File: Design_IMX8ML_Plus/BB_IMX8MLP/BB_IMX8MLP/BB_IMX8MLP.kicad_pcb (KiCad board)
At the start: 2 copper layers, 125 x 100 mm, 207 parts, among them J1 DF40C-100DP-0.4V_51_, J10 Barrel_Jack, J11 SIM_Card, J2 DF40C-100DP-0.4V_51_, J3 DF40C-100DP-0.4V_51_, J4 DF40C-100DP-0.4V_51_, J5 RJ45_JK0654219, J6 RJ45_JK0654219, J7 HDMI_A, J8 Bus_PCI_Express_Mini, J9 GSB311231HR, Q1 PMDT290UCE, Q2 NTMFS5C670NLT1G, Q3 NTMFS5C670NLT1G, Q4 PMDT290UCE, SW1 Power ON/OFF, SW2 RESET, SW3 RECOVERY, U1 KSZ9131RNXI, U10 PCMF3USB3S, U17 FXMA2102L8X, U2 HDMI2C1-14HDS, U20 INA219BxD, U21 PCMF3USB3S, U22 PCMF3USB3S, U23 PCMF3USB3S, U3 USB5744_2G, U30 NAU88C22YG, U4 LTC4368IDD-1_PBF, U5 AOZ2261AQI-15, U6 NCV4274CST50T3G, U7 AOZ2261AQI-15, U8 LTC2954CDDB-1-TRMPBF, U9 PCMF3USB3S, Y1 25MHz, Y2 25MHz

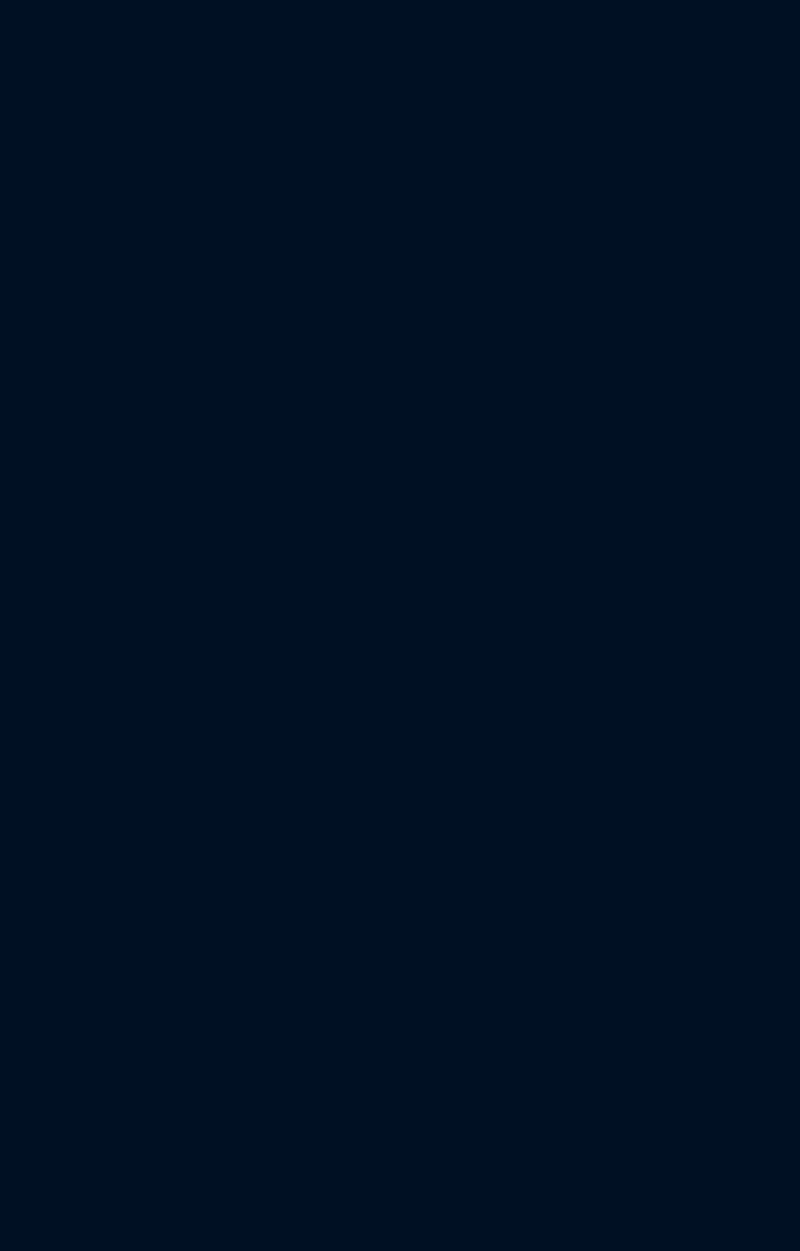
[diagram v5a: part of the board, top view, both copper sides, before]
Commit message: Adds audio interface
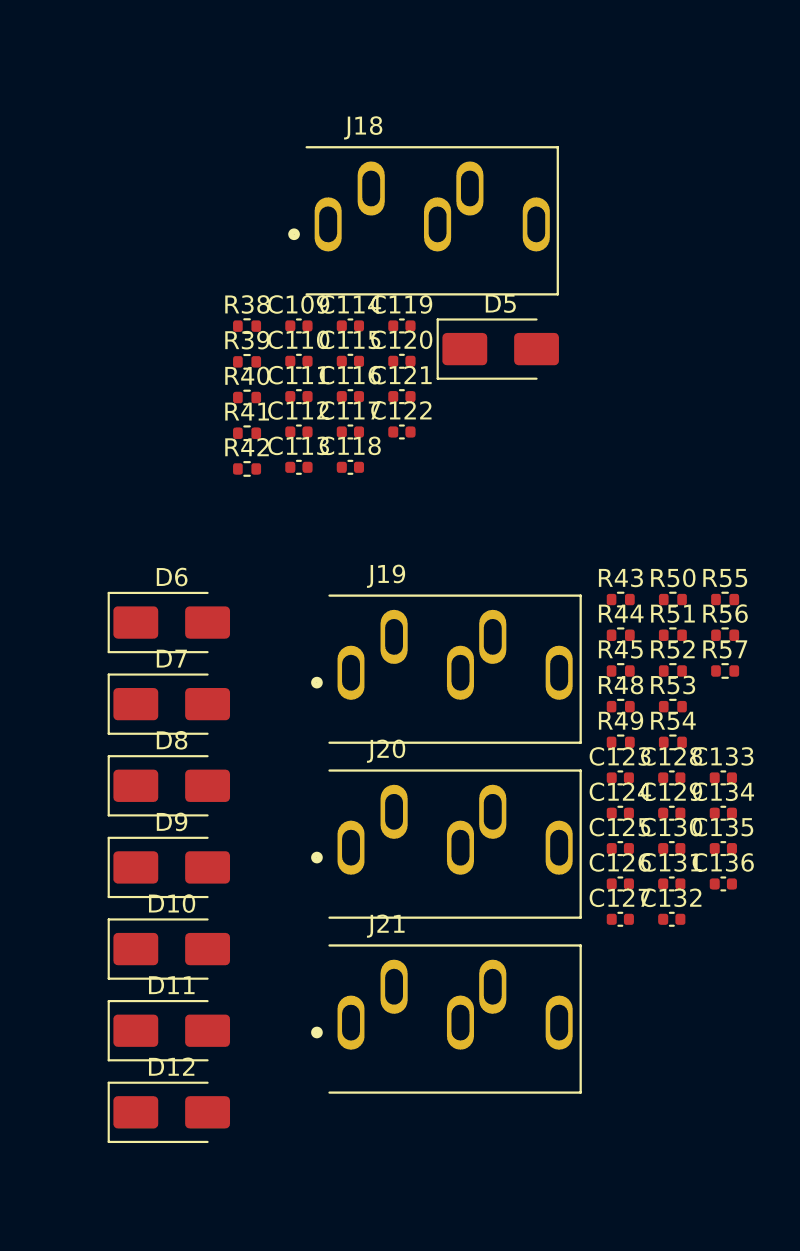
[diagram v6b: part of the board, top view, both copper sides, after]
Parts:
- added C109: 220pF, Capacitor_SMD:C_0402_1005Metric, F.Cu at (250.7, 74.9)
- added C110: 100nF, Capacitor_SMD:C_0402_1005Metric, F.Cu at (250.7, 76.8)
- added C111: 100nF, Capacitor_SMD:C_0402_1005Metric, F.Cu at (250.7, 78.8)
- added C112: 4.7uF, Capacitor_SMD:C_0402_1005Metric, F.Cu at (250.7, 80.8)
- added C113: 100nF, Capacitor_SMD:C_0402_1005Metric, F.Cu at (250.7, 82.7)
- added C114: 4.7uF, Capacitor_SMD:C_0402_1005Metric, F.Cu at (253.5, 74.9)
- added C115: 4.7uF, Capacitor_SMD:C_0402_1005Metric, F.Cu at (253.5, 76.8)
- added C116: 4.7uF, Capacitor_SMD:C_0402_1005Metric, F.Cu at (253.5, 78.8)
- added C117: 100nF, Capacitor_SMD:C_0402_1005Metric, F.Cu at (253.5, 80.8)
- added C118: 100nF, Capacitor_SMD:C_0402_1005Metric, F.Cu at (253.5, 82.7)
- added C119: 4.7uF, Capacitor_SMD:C_0402_1005Metric, F.Cu at (256.4, 74.9)
- added C120: 100nF, Capacitor_SMD:C_0402_1005Metric, F.Cu at (256.4, 76.8)
- added C121: 100nF, Capacitor_SMD:C_0402_1005Metric, F.Cu at (256.4, 78.8)
- added C122: 4.7uF, Capacitor_SMD:C_0402_1005Metric, F.Cu at (256.4, 80.8)
- added C123: 220pF, Capacitor_SMD:C_0402_1005Metric, F.Cu at (268.6, 100.0)
- added C124: 220pF, Capacitor_SMD:C_0402_1005Metric, F.Cu at (268.6, 102.0)
- added C125: 220pF, Capacitor_SMD:C_0402_1005Metric, F.Cu at (268.6, 104.0)
- added C126: 220pF, Capacitor_SMD:C_0402_1005Metric, F.Cu at (268.6, 106.0)
- added C127: 220pF, Capacitor_SMD:C_0402_1005Metric, F.Cu at (268.6, 107.9)
- added C128: 220pF, Capacitor_SMD:C_0402_1005Metric, F.Cu at (271.5, 100.0)
- added C129: 220pF, Capacitor_SMD:C_0402_1005Metric, F.Cu at (271.5, 102.0)
- added C130: 220pF, Capacitor_SMD:C_0402_1005Metric, F.Cu at (271.5, 104.0)
- added C131: 1uF, Capacitor_SMD:C_0402_1005Metric, F.Cu at (271.5, 106.0)
- added C132: 1uf, Capacitor_SMD:C_0402_1005Metric, F.Cu at (271.5, 107.9)
- added C133: 1uf, Capacitor_SMD:C_0402_1005Metric, F.Cu at (274.3, 100.0)
- added C134: 1uF, Capacitor_SMD:C_0402_1005Metric, F.Cu at (274.3, 102.0)
- added C135: 1uf, Capacitor_SMD:C_0402_1005Metric, F.Cu at (274.3, 104.0)
- added C136: 1uF, Capacitor_SMD:C_0402_1005Metric, F.Cu at (274.3, 106.0)
- added D10: SS3200, Diode_SMD:D_SMA, F.Cu at (243.6, 109.6)
- added D11: SS3200, Diode_SMD:D_SMA, F.Cu at (243.6, 114.1)
- added D12: SS3200, Diode_SMD:D_SMA, F.Cu at (243.6, 118.7)
- added D5: SS3200, Diode_SMD:D_SMA, F.Cu at (261.9, 76.2)
- added D6: SS3200, Diode_SMD:D_SMA, F.Cu at (243.6, 91.4)
- added D7: SS3200, Diode_SMD:D_SMA, F.Cu at (243.6, 95.9)
- added D8: SS3200, Diode_SMD:D_SMA, F.Cu at (243.6, 100.5)
- added D9: SS3200, Diode_SMD:D_SMA, F.Cu at (243.6, 105.0)
- added J18: MIC IN-Pink, _W_SBC:SJ1-3535NG-PI, F.Cu at (252.3, 69.2)
- added J19: Head Out -Green, _W_SBC:SJ1-3535NG-PI, F.Cu at (253.6, 94.2)
- added J20: Line -in -Blue, _W_SBC:SJ1-3535NG-PI, F.Cu at (253.6, 103.9)
- added J21: AUX OUT -Black, _W_SBC:SJ1-3535NG-PI, F.Cu at (253.6, 113.7)
- added R38: 47K, Resistor_SMD:R_0402_1005Metric, F.Cu at (247.8, 74.9)
- added R39: 120R@100MHz, Resistor_SMD:R_0402_1005Metric, F.Cu at (247.8, 76.9)
- added R40: 120R@100MHz, Resistor_SMD:R_0402_1005Metric, F.Cu at (247.8, 78.8)
- added R41: 120R@100MHz, Resistor_SMD:R_0402_1005Metric, F.Cu at (247.8, 80.8)
- added R42: 120R@100MHz, Resistor_SMD:R_0402_1005Metric, F.Cu at (247.8, 82.8)
- added R43: 47k, Resistor_SMD:R_0402_1005Metric, F.Cu at (268.6, 90.1)
- added R44: 2.2k, Resistor_SMD:R_0402_1005Metric, F.Cu at (268.6, 92.1)
- added R45: 2.2K, Resistor_SMD:R_0402_1005Metric, F.Cu at (268.6, 94.1)
- added R48: 47k, Resistor_SMD:R_0402_1005Metric, F.Cu at (268.6, 96.1)
- added R49: 47K, Resistor_SMD:R_0402_1005Metric, F.Cu at (268.6, 98.1)
- added R50: 100, Resistor_SMD:R_0402_1005Metric, F.Cu at (271.5, 90.1)
- added R51: 100, Resistor_SMD:R_0402_1005Metric, F.Cu at (271.5, 92.1)
- added R52: 4.7k, Resistor_SMD:R_0402_1005Metric, F.Cu at (271.5, 94.1)
- added R53: 4.7K, Resistor_SMD:R_0402_1005Metric, F.Cu at (271.5, 96.1)
- added R54: 10k, Resistor_SMD:R_0402_1005Metric, F.Cu at (271.5, 98.1)
- added R55: 10K, Resistor_SMD:R_0402_1005Metric, F.Cu at (274.4, 90.1)
- added R56: 100, Resistor_SMD:R_0402_1005Metric, F.Cu at (274.4, 92.1)
- added R57: 100, Resistor_SMD:R_0402_1005Metric, F.Cu at (274.4, 94.1)
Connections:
- U30 pad 12: unconnected-(U30-VSSD-Pad12) -> LVDS0_D2_N
- U30 pad 13: unconnected-(U30-VDDC-Pad13) -> /Audio/1v8_AAP
- U30 pad 14: unconnected-(U30-VDDB-Pad14) -> /Audio/1v8_AAP
- U30 pad 24: unconnected-(U30-VSSSPK-Pad24) -> LVDS0_D2_N
- U30 pad 26: unconnected-(U30-VDDSPK-Pad26) -> /Audio/3v3_AAP
- U30 pad 28: unconnected-(U30-VSSA-Pad28) -> LVDS0_D2_N
- U30 pad 31: unconnected-(U30-VDDA-Pad31) -> /Audio/3v3_AAP
- U30 pad 33: unconnected-(U30-EXP-Pad33) -> LVDS0_D2_N

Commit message: Review
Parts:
- added C137: 1uf, Capacitor_SMD:C_0402_1005Metric, F.Cu at (24.9, 10.4)
- added C138: 1uF, Capacitor_SMD:C_0402_1005Metric, F.Cu at (24.9, 12.4)
- added C139: 100nF, Capacitor_SMD:C_0402_1005Metric, F.Cu at (12.2, 12.4)
- added C140: 10uF, Capacitor_SMD:C_0402_1005Metric, F.Cu at (12.2, 14.4)
- added C141: 100nF, Capacitor_SMD:C_0402_1005Metric, F.Cu at (12.2, 16.4)
- added C142: 100nF, Capacitor_SMD:C_0402_1005Metric, F.Cu at (17.1, 0.48)
- added C143: 100nF, Capacitor_SMD:C_0402_1005Metric, F.Cu at (17.1, 2.46)
- added C144: 100nF, Capacitor_SMD:C_0402_1005Metric, F.Cu at (17.1, 4.42)
- added C145: 100nF, Capacitor_SMD:C_0402_1005Metric, F.Cu at (17.1, 6.39)
- added C146: 100nF, Capacitor_SMD:C_0402_1005Metric, F.Cu at (17.1, 8.37)
- added C147: 100nF, Capacitor_SMD:C_0402_1005Metric, F.Cu at (17.1, 10.3)
- added C148: 100nF, Capacitor_SMD:C_0402_1005Metric, F.Cu at (17.1, 12.3)
- added C149: 100nF, Capacitor_SMD:C_0402_1005Metric, F.Cu at (17.1, 14.3)
- added C150: 100nF, Capacitor_SMD:C_0402_1005Metric, F.Cu at (17.1, 18.2)
- added C151: 100nF, Capacitor_SMD:C_0402_1005Metric, F.Cu at (17.1, 20.2)
- added C152: 100nF, Capacitor_SMD:C_0402_1005Metric, F.Cu at (17.1, 22.2)
- added C153: 100nF, Capacitor_SMD:C_0402_1005Metric, F.Cu at (17.1, 24.2)
- added C154: 100pF, Capacitor_SMD:C_0402_1005Metric, F.Cu at (24.9, 18.2)
- added C155: 1nF, Capacitor_SMD:C_0402_1005Metric, F.Cu at (24.9, 20.2)
- added C156: 100nF, Capacitor_SMD:C_0402_1005Metric, F.Cu at (24.9, 22.2)
- added R46: 10k, Resistor_SMD:R_0402_1005Metric, F.Cu at (12.2, 18.4)
- added R47: 10K, Resistor_SMD:R_0402_1005Metric, F.Cu at (20.0, 0.49)
- added R58: 6.04k, Resistor_SMD:R_0402_1005Metric, F.Cu at (20.0, 2.48)
- added R59: 0, Resistor_SMD:R_0402_1005Metric, F.Cu at (20.0, 18.3)
- added R60: 0, Resistor_SMD:R_0402_1005Metric, F.Cu at (20.0, 20.2)
- added R61: 0, Resistor_SMD:R_0402_1005Metric, F.Cu at (20.0, 22.2)
- added R62: 10K, Resistor_SMD:R_0402_1005Metric, F.Cu at (27.8, 18.3)
- added R63: 10K, Resistor_SMD:R_0402_1005Metric, F.Cu at (27.8, 20.2)
- added R64: 10K, Resistor_SMD:R_0402_1005Metric, F.Cu at (24.9, 0.49)
- added R65: 10K, Resistor_SMD:R_0402_1005Metric, F.Cu at (24.9, 2.48)
- added R66: 10K, Resistor_SMD:R_0402_1005Metric, F.Cu at (24.9, 4.47)
- added R67: 10K, Resistor_SMD:R_0402_1005Metric, F.Cu at (24.9, 6.46)
- added U31: FT4232H, Package_DFN_QFN:VQFN-64-1EP_9x9mm_P0.5mm_EP5.4x5.4mm, F.Cu at (5.12, 17.1)
- added U33: TJA1052i-1, Package_SO:SOIC-16W_7.5x10.3mm_P1.27mm, F.Cu at (5.96, 5.54)
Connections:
- net /PCIe/1V5_PCIe renamed /PCIe_SDCard/1V5_PCIe
- net /PCIe/3V3_PCIe renamed /PCIe_SDCard/3V3_PCIe
- net /PCIe/PCIe_CLK renamed /PCIe_SDCard/PCIe_CLK
- net /PCIe/PCIe_SDA renamed /PCIe_SDCard/PCIe_SDA
- net Net-(C62-Pad1) renamed /USB/usb_connectors/VBUS
- net Net-(U16-VCCA) renamed /USB/1v8
- net Net-(U18-VCCA) renamed /PCIe_SDCard/1v8
- net Net-(U18-VCCB) renamed /PCIe_SDCard/3v3
- net Net-(U19-VCCA) renamed /CSI_DSI/1v8
- net Net-(U19-VCCB) renamed /CSI_DSI/3v3
- C131 pad 1: unconnected-(C131-Pad1) -> /Audio/AUXOUT1
- C132 pad 1: unconnected-(C132-Pad1) -> /Audio/AUXOUT2
- C133 pad 1: unconnected-(C133-Pad1) -> /Audio/LAUXIN
- C134 pad 1: unconnected-(C134-Pad1) -> /Audio/RAUXIN
- C135 pad 1: unconnected-(C135-Pad1) -> /Audio/LHP
- C136 pad 1: unconnected-(C136-Pad1) -> /Audio/RHP
- C48 pad 1: Net-(C48-Pad1) -> /USB/usb_connectors/VBUSH_1
- C49 pad 1: Net-(C48-Pad1) -> /USB/usb_connectors/VBUSH_1
- C50 pad 1: Net-(C48-Pad1) -> /USB/usb_connectors/VBUSH_1
- C56 pad 1: Net-(C56-Pad1) -> /USB/usb_connectors/VBUSH_2
- C57 pad 1: Net-(C56-Pad1) -> /USB/usb_connectors/VBUSH_2
- C58 pad 1: Net-(C56-Pad1) -> /USB/usb_connectors/VBUSH_2
- C74 pad 1: Net-(U16-VCCB) -> /USB/3v3
- FB1 pad 2: Net-(C48-Pad1) -> /USB/usb_connectors/VBUSH_1
- FB2 pad 2: Net-(C56-Pad1) -> /USB/usb_connectors/VBUSH_2
- J5 pad 1: unconnected-(J5-MXCT3-Pad1) -> Net-(J5-MXCT3)
- J5 pad 12: unconnected-(J5-MXCT1-Pad12) -> Net-(J5-MXCT1)
- J5 pad 14: unconnected-(J5-LED2+-Pad14) -> /Ethernet/3v3
- J5 pad 16: unconnected-(J5-LED1+-Pad16) -> /Ethernet/3v3
- J5 pad 6: unconnected-(J5-MXCT2-Pad6) -> Net-(J5-MXCT2)
- J5 pad 7: unconnected-(J5-MXCT4-Pad7) -> Net-(J5-MXCT4)
- J6 pad 1: unconnected-(J6-MXCT3-Pad1) -> Net-(J6-MXCT3)
- J6 pad 12: unconnected-(J6-MXCT1-Pad12) -> Net-(J6-MXCT1)
- J6 pad 14: unconnected-(J6-LED2+-Pad14) -> /Ethernet/3v3
- J6 pad 16: unconnected-(J6-LED1+-Pad16) -> /Ethernet/3v3
- J6 pad 6: unconnected-(J6-MXCT2-Pad6) -> Net-(J6-MXCT2)
- J6 pad 7: unconnected-(J6-MXCT4-Pad7) -> Net-(J6-MXCT4)
- J9 pad 1: unconnected-(J9A-VBUS_1-Pad1) -> /USB/usb_connectors/VBUSH_1
- J9 pad 10: unconnected-(J9B-VBUS_2-Pad10) -> /USB/usb_connectors/VBUSH_2
- U1 pad 41: unconnected-(U1A-CLK125_NDO/LED_MODE-Pad41) -> /Ethernet/LED_MODE
- U1 pad 48: unconnected-(U1A-ISET-Pad48) -> /Ethernet/ISET
- U10 pad A5: USBH2_SSTX- -> Net-(U10C-CH3_IN+)
- U10 pad A6: USBH2_SSTX+ -> Net-(U10C-CH3_IN-)
- U11 pad 4: unconnected-(U11-FLTB-Pad4) -> Net-(U11-FLTB)
- U11 pad 8: unconnected-(U11-ILIM-Pad8) -> USBH3_PRT_CTL
- U12 pad 4: unconnected-(U12-FLTB-Pad4) -> Net-(U12-FLTB)
- U12 pad 8: unconnected-(U12-ILIM-Pad8) -> USBH2_PRT_CTL
- U13 pad 4: unconnected-(U13-FLTB-Pad4) -> Net-(U13-FLTB)
- U13 pad 8: unconnected-(U13-ILIM-Pad8) -> Net-(U13-ILIM)
- U16 pad 2: unconnected-(U16-A0-Pad2) -> /USB/I2C1_SCL
- U16 pad 3: unconnected-(U16-A1-Pad3) -> /USB/I2C1_SDA
- U16 pad 6: unconnected-(U16-B1-Pad6) -> /USB/I2C1_USBH_SDA
- U16 pad 7: unconnected-(U16-B0-Pad7) -> /USB/I2C1_USBH_SCL
- U16 pad 8: Net-(U16-VCCB) -> /USB/3v3
- U18 pad 2: unconnected-(U18-A0-Pad2) -> /PCIe_SDCard/I2C1_SCL
- U18 pad 3: unconnected-(U18-A1-Pad3) -> /PCIe_SDCard/I2C1_SDA
- U19 pad 2: unconnected-(U19-A0-Pad2) -> /CSI_DSI/I2C1_SCL
- U19 pad 3: unconnected-(U19-A1-Pad3) -> /CSI_DSI/I2C1_SDA
- U19 pad 6: unconnected-(U19-B1-Pad6) -> /CSI_DSI/I2C1_DTA_LVDS0
- U19 pad 7: unconnected-(U19-B0-Pad7) -> /CSI_DSI/I2C1_SCL_LVDS0
- U30 pad 1: unconnected-(U30-LMICP-Pad1) -> /Audio/LMIC_P
- U30 pad 18: unconnected-(U30-MODE-Pad18) -> LVDS0_D2_N
- U30 pad 19: unconnected-(U30-LAUXIN-Pad19) -> /Audio/LAUXIN
- U30 pad 2: unconnected-(U30-LMICN-Pad2) -> /Audio/LMIC_N
- U30 pad 20: unconnected-(U30-RAUXIN-Pad20) -> /Audio/RAUXIN
- U30 pad 21: unconnected-(U30-AUXOUT1-Pad21) -> /Audio/AUXOUT1
- U30 pad 22: unconnected-(U30-AUXOUT2-Pad22) -> /Audio/AUXOUT2
- U30 pad 23: unconnected-(U30-RSPKOUT-Pad23) -> /Audio/RSPKOUT
- U30 pad 25: unconnected-(U30-LSPKOUT-Pad25) -> /Audio/LSPKOUT
- U30 pad 29: unconnected-(U30-RHP-Pad29) -> /Audio/RHP
- U30 pad 3: unconnected-(U30-LLIN/GPIO2-Pad3) -> /Audio/LLIN-GPIO2
- U30 pad 30: unconnected-(U30-LHP-Pad30) -> /Audio/LHP
- U30 pad 32: unconnected-(U30-MICBIAS-Pad32) -> /Audio/MICBIAS
- U30 pad 4: unconnected-(U30-RMICP-Pad4) -> /Audio/RMIC_P
- U30 pad 5: unconnected-(U30-RMICN-Pad5) -> /Audio/RMIC_N
- U30 pad 6: unconnected-(U30-RLIN/GPIO3-Pad6) -> /Audio/RLIN-GPIO3
- U9 pad A3: USBH3_SSTX- -> Net-(U9B-CH2_IN+)
- U9 pad A4: USBH3_SSTX+ -> Net-(U9B-CH2_IN-)

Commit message: reorganization of the componentes
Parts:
- removed Q1, Q4: PMDT290UCE, Package_TO_SOT_SMD:SOT-666
- added C157: 10uF, Capacitor_SMD:C_0402_1005Metric, F.Cu at (-226.1, 227.3)
- added C158: 100nF, Capacitor_SMD:C_0402_1005Metric, F.Cu at (-225.8, 234.8)
- added C159: 10uF, Capacitor_SMD:C_0402_1005Metric, F.Cu at (-248.5, 230.2)
- added C160: 100nF, Capacitor_SMD:C_0402_1005Metric, F.Cu at (-247.4, 230.2)
- added C161: 4.7uF, Capacitor_SMD:C_0402_1005Metric, F.Cu at (-254.9, 368.3)
- added C162: 4.7uF, Capacitor_SMD:C_0402_1005Metric, F.Cu at (-246.2, 378.4)
- added C163: 100nF, Capacitor_SMD:C_0402_1005Metric, F.Cu at (-237.6, 225.5)
- added C164: 100nF, Capacitor_SMD:C_0402_1005Metric, F.Cu at (-230.5, 232.3)
- added C165: 100nF, Capacitor_SMD:C_0402_1005Metric, F.Cu at (-234.7, 240.0)
- added C166: 100nF, Capacitor_SMD:C_0402_1005Metric, F.Cu at (-240.2, 240.2)
- added C167: 100nF, Capacitor_SMD:C_0402_1005Metric, F.Cu at (-253.7, 368.3)
- added C168: 4.7uF, Capacitor_SMD:C_0402_1005Metric, F.Cu at (-245.6, 356.5)
- added C169: 4.7uF, Capacitor_SMD:C_0402_1005Metric, F.Cu at (-255.8, 346.5)
- added C170: 100nF, Capacitor_SMD:C_0402_1005Metric, F.Cu at (-247.8, 232.8)
- added C171: 100nF, Capacitor_SMD:C_0402_1005Metric, F.Cu at (-234.8, 225.8)
- added C172: 12Pf, Capacitor_SMD:C_0402_1005Metric, F.Cu at (-257.9, 223.7)
- added C173: 12Pf, Capacitor_SMD:C_0402_1005Metric, F.Cu at (-258.1, 231.8)
- added C174: 100nF, Capacitor_SMD:C_0402_1005Metric, F.Cu at (-240.1, 217.6)
- added C175: 100nF, Capacitor_SMD:C_0402_1005Metric, F.Cu at (-253.4, 383.1)
- added C176: 100nF, Capacitor_SMD:C_0402_1005Metric, F.Cu at (-245.0, 385.1)
- added C177: 100nF, Capacitor_SMD:C_0402_1005Metric, F.Cu at (-246.1, 385.2)
- added C178: 100nF, Capacitor_SMD:C_0402_1005Metric, F.Cu at (-266.3, 351.2)
- added C179: 100nF, Capacitor_SMD:C_0402_1005Metric, F.Cu at (-255.4, 352.2)
- added C180: 100nF, Capacitor_SMD:C_0402_1005Metric, F.Cu at (-256.4, 352.2)
- added C181: 100nF, Capacitor_SMD:C_0402_1005Metric, F.Cu at (-233.3, 226.3)
- added C182: 100nF, Capacitor_SMD:C_0402_1005Metric, F.Cu at (-246.5, 234.7)
- added C183: 100nF, Capacitor_SMD:C_0402_1005Metric, F.Cu at (-230.5, 234.9)
- added C184: 100nF, Capacitor_SMD:C_0402_1005Metric, F.Cu at (-241.7, 225.4)
- added C185: 10uF, Capacitor_SMD:C_0402_1005Metric, F.Cu at (-250.2, 226.7)
- added C186: 100nF, Capacitor_SMD:C_0402_1005Metric, F.Cu at (-249.2, 226.7)
- added C187: 100nF, Capacitor_SMD:C_0402_1005Metric, F.Cu at (-254.6, 346.5)
- added C188: 10uF, Capacitor_SMD:C_1210_3225Metric_Pad1.33x2.70mm_HandSolder, F.Cu at (42.6, 37.4)
- added J12: CAM_1, Connector_FFC-FPC:Hirose_FH12-24S-0.5SH_1x24-1MP_P0.50mm_Horizontal, F.Cu at (335.0, 237.2)
- added J13: CAM_2, Connector_FFC-FPC:Hirose_FH12-24S-0.5SH_1x24-1MP_P0.50mm_Horizontal, F.Cu at (335.4, 250.8)
- added J14: USB_C_Receptacle, Connector_USB:USB_C_Receptacle_GCT_USB4110, F.Cu at (270.0, 239.0)
- added J15: DSI, Connector_FFC-FPC:Hirose_FH12-24S-0.5SH_1x24-1MP_P0.50mm_Horizontal, F.Cu at (315.2, 237.2)
- added J22: SD_Card_Receptacle, Connector_Card:SD_Hirose_DM1AA_SF_PEJ82, F.Cu at (377.8, 285.5)
- added J23: USB_C_Receptacle, Connector_USB:USB_C_Receptacle_GCT_USB4110, F.Cu at (-237.4, 255.9)
- added J24: CAN_1, Connector_PinSocket_2.54mm:PinSocket_1x04_P2.54mm_Vertical, F.Cu at (-235.9, 374.8)
- added J25: CAN_2, Connector_PinSocket_2.54mm:PinSocket_1x04_P2.54mm_Vertical, F.Cu at (-236.8, 353.8)
- added J26: LVDS, Connector_PinHeader_1.00mm:PinHeader_2x20_P1.00mm_Vertical_SMD, F.Cu at (351.6, 242.5)
- added L5: 120R@10MHz, Inductor_SMD:L_0805_2012Metric, F.Cu at (-247.8, 226.1)
- added L6: 120R@10MHz, Inductor_SMD:L_0805_2012Metric, F.Cu at (-250.0, 231.0)
- added R68: 10k, Resistor_SMD:R_0402_1005Metric, F.Cu at (-226.1, 228.3)
- added R69: 12k, Resistor_SMD:R_0402_1005Metric, F.Cu at (-246.5, 235.7)
- added R70: 10k, Resistor_SMD:R_0402_1005Metric, F.Cu at (-247.8, 231.7)
- added R71: 1M, Resistor_SMD:R_0402_1005Metric, F.Cu at (-254.8, 227.9)
- added R72: 150, Resistor_SMD:R_0402_1005Metric, F.Cu at (-254.3, 229.4)
- added R73: 150, Resistor_SMD:R_0402_1005Metric, F.Cu at (-237.4, 223.2)
- added R74: 10k, Resistor_SMD:R_0402_1005Metric, F.Cu at (-239.4, 222.8)
- added R75: 10k, Resistor_SMD:R_0402_1005Metric, F.Cu at (-236.7, 222.1)
- added R76: 10k, Resistor_SMD:R_0402_1005Metric, F.Cu at (-240.1, 220.0)
- added R77: 5.1k, Resistor_SMD:R_0402_1005Metric, F.Cu at (-232.9, 249.5)
- added R78: 5.1k, Resistor_SMD:R_0402_1005Metric, F.Cu at (-240.3, 249.1)
- added R79: 0.01, Resistor_SMD:R_1206_3216Metric_Pad1.30x1.75mm_HandSolder, F.Cu at (45.8, 55.8)
- added U32: ~, Package_DFN_QFN:UQFN-16_1.8x2.6mm_P0.4mm, F.Cu at (-237.1, 243.7)
- added U34: ~, Package_DFN_QFN:UQFN-16_1.8x2.6mm_P0.4mm, F.Cu at (-225.6, 231.5)
- added U35: 93LCxxB, Package_DFN_QFN:DFN-8-1EP_3x2mm_P0.5mm_EP1.7x1.4mm, F.Cu at (-238.2, 218.8)
- added U36: ~, Package_TO_SOT_SMD:SOT-23-3, F.Cu at (-254.7, 356.5)
- added U38: ISO1044BD, Package_SO:SOIC-8_3.9x4.9mm_P1.27mm, F.Cu at (-250.8, 386.7)
- added U40: PCMF3USB3S, Package_CSP:Nexperia_WLCSP-15_6-3-6_2.37x1.17mm_Layout6x3_P0.4mm, F.Cu at (-6.03, 13.8)
- added U41: PCMF3USB3S, Package_CSP:Nexperia_WLCSP-15_6-3-6_2.37x1.17mm_Layout6x3_P0.4mm, F.Cu at (-6.03, 18.0)
- added U42: NTE0505MC, _W_SBC:NTE_SINGLE_M_MUR-L, F.Cu at (-246.1, 371.0)
- added U43: NTE0505MC, _W_SBC:NTE_SINGLE_M_MUR-L, F.Cu at (-245.7, 349.0)
- added Y3: 12MHz, Crystal:Crystal_SMD_0603-4Pin_6.0x3.5mm, F.Cu at (-258.2, 227.8)
- C10, C8, R14, U6: moved to F.Cu
- C139: value 100nF -> 10uF; footprint Capacitor_SMD:C_0402_1005Metric -> Capacitor_SMD:C_1210_3225Metric_Pad1.33x2.70mm_HandSolder
- C14, C15, C16: footprint Capacitor_SMD:C_0402_1005Metric -> Capacitor_SMD:C_1210_3225Metric_Pad1.33x2.70mm_HandSolder
- C142, C143, C144, C145, C146, C147, C148, C149, R10, R11, U24, U25: moved to B.Cu
- C20: footprint Capacitor_SMD:C_0402_1005Metric -> Capacitor_SMD:C_1210_3225Metric
- C5: value 10uF -> 2.2nF; footprint Capacitor_SMD:C_0402_1005Metric -> Capacitor_SMD:C_0805_2012Metric_Pad1.18x1.45mm_HandSolder; moved to F.Cu
- C6: value 10uF -> 100nF
- F1: footprint Fuse:Fuse_0603_1608Metric -> Fuse:Fuse_1210_3225Metric_Pad1.42x2.65mm_HandSolder
- R1, R2: value 100K -> 10; moved to F.Cu
- R16: value 100K -> 0
- R17: value 100K -> 100
- R27: value 47K -> 100
- U33: value TJA1052i-1 -> ISO1044BD; footprint Package_SO:SOIC-16W_7.5x10.3mm_P1.27mm -> Package_SO:SOIC-8_3.9x4.9mm_P1.27mm
- moved R27 522.6 mm to (-239.2, 377.4), turned to 180 degrees
- moved C144 466.6 mm to (352.1, 329.2), turned to -90 degrees
- moved C145 464.7 mm to (353.8, 326.7), turned to -90 degrees
- moved C143 461.0 mm to (342.0, 329.4), turned to -90 degrees
- moved C142 459.0 mm to (340.2, 326.5), turned to -90 degrees
- moved C148 446.7 mm to (332.2, 328.9), turned to -90 degrees
- moved R58 446.0 mm to (342.5, 310.6), turned to 90 degrees
- moved C149 445.1 mm to (334.1, 326.7), turned to -90 degrees
- moved R47 443.6 mm to (342.1, 305.5), turned to -90 degrees
- moved C147 441.0 mm to (321.9, 329.0), turned to -90 degrees
- moved U33 439.2 mm to (-261.8, 353.7)
- moved C146 438.9 mm to (319.7, 326.3), turned to -90 degrees
- moved C91 411.1 mm to (352.9, 290.2), turned to -90 degrees
- moved C99 409.1 mm to (351.2, 298.5), turned to -90 degrees
- moved C92 409.0 mm to (351.8, 290.2), turned to -90 degrees
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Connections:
- net Net-(U17-VCCA) renamed /power_unit/power_5v/1v8
- net Net-(U4-VIN) renamed /power_unit/V_IN
- C1 pad 2: LVDS0_D2_N -> GND
- C10 pad 1: /power_unit/+V_SUPPLY_FILT -> +V_SUPPLY_FILT
- C10 pad 2: LVDS0_D2_N -> GND
- C100 pad 2: LVDS0_D2_N -> GND
- C101 pad 1: Net-(U20-VS) -> /power_unit/power_5v/3v3
- C101 pad 2: LVDS0_D2_N -> GND
- C103 pad 2: LVDS0_D2_N -> GND
- C104 pad 2: LVDS0_D2_N -> GND
- C105 pad 2: LVDS0_D2_N -> GND
- C106 pad 2: LVDS0_D2_N -> GND
- C107 pad 2: LVDS0_D2_N -> GND
- C108 pad 2: LVDS0_D2_N -> GND
- C109 pad 2: LVDS0_D2_N -> GND
- C11 pad 1: /power_unit/+V5_STB -> +V5_STB
- C11 pad 2: LVDS0_D2_N -> GND
- C110 pad 2: LVDS0_D2_N -> GND
- C111 pad 2: LVDS0_D2_N -> GND
- C112 pad 2: LVDS0_D2_N -> GND
- C113 pad 2: LVDS0_D2_N -> GND
- C114 pad 2: LVDS0_D2_N -> GND
- C115 pad 2: LVDS0_D2_N -> GND
- C116 pad 2: LVDS0_D2_N -> GND
- C117 pad 2: LVDS0_D2_N -> GND
- C118 pad 2: LVDS0_D2_N -> GND
- C119 pad 2: LVDS0_D2_N -> GND
- C12 pad 1: /power_unit/+V5_STB -> +V5_STB
- C12 pad 2: LVDS0_D2_N -> GND
- C120 pad 2: LVDS0_D2_N -> GND
- C121 pad 2: LVDS0_D2_N -> GND
- C122 pad 2: LVDS0_D2_N -> GND
- C123 pad 2: LVDS0_D2_N -> GND
- C124 pad 2: LVDS0_D2_N -> GND
- C125 pad 2: LVDS0_D2_N -> GND
- C126 pad 2: LVDS0_D2_N -> GND
- C127 pad 2: LVDS0_D2_N -> GND
- C128 pad 2: LVDS0_D2_N -> GND
- C129 pad 2: LVDS0_D2_N -> GND
- C13 pad 2: LVDS0_D2_N -> GND
- C130 pad 2: LVDS0_D2_N -> GND
- C139 pad 1: unconnected-(C139-Pad1) -> +V_SUPPLY_FILT
- C139 pad 2: LVDS0_D2_N -> GND
- C14 pad 1: /power_unit/+V_SUPPLY_FILT -> +V_SUPPLY_FILT
- C14 pad 2: LVDS0_D2_N -> GND
- C141 pad 2: LVDS0_D2_N -> GND
- C142 pad 2: LVDS0_D2_N -> GND
- C143 pad 2: LVDS0_D2_N -> GND
- C144 pad 2: LVDS0_D2_N -> GND
- C145 pad 2: LVDS0_D2_N -> GND
- C146 pad 2: LVDS0_D2_N -> GND
- C147 pad 2: LVDS0_D2_N -> GND
- C148 pad 2: LVDS0_D2_N -> GND
- C149 pad 2: LVDS0_D2_N -> GND
- C15 pad 1: /power_unit/+V_SUPPLY_FILT -> +V_SUPPLY_FILT
- C15 pad 2: LVDS0_D2_N -> GND
- C154 pad 1: /PCIe_SDCard/3v3 -> Net-(C154-Pad1)
- C154 pad 2: LVDS0_D2_N -> GND
- C155 pad 1: /PCIe_SDCard/3v3 -> Net-(C154-Pad1)
- C155 pad 2: LVDS0_D2_N -> GND
- C156 pad 1: /PCIe_SDCard/3v3 -> Net-(C154-Pad1)
- C156 pad 2: LVDS0_D2_N -> GND
- C16 pad 1: /power_unit/+V_SUPPLY_FILT -> +V_SUPPLY_FILT
- C16 pad 2: LVDS0_D2_N -> GND
- C17 pad 2: LVDS0_D2_N -> GND
- C19 pad 2: LVDS0_D2_N -> GND
- C2 pad 2: LVDS0_D2_N -> GND
- C20 pad 2: LVDS0_D2_N -> GND
- C21 pad 2: LVDS0_D2_N -> GND
- C22 pad 2: LVDS0_D2_N -> GND
- C23 pad 2: LVDS0_D2_N -> GND
- C24 pad 2: LVDS0_D2_N -> GND
- C25 pad 2: LVDS0_D2_N -> GND
- C27 pad 2: LVDS0_D2_N -> GND
- C28 pad 2: LVDS0_D2_N -> GND
- C29 pad 2: LVDS0_D2_N -> GND
- C3 pad 1: VDD_SYS -> /power_unit/power_5v/5v
- C3 pad 2: LVDS0_D2_N -> GND
- C30 pad 2: LVDS0_D2_N -> GND
- C31 pad 2: LVDS0_D2_N -> GND
- C32 pad 2: LVDS0_D2_N -> GND
- C33 pad 2: LVDS0_D2_N -> GND
- C34 pad 2: LVDS0_D2_N -> GND
- C35 pad 2: LVDS0_D2_N -> GND
- C36 pad 2: LVDS0_D2_N -> GND
- C37 pad 2: LVDS0_D2_N -> GND
- C38 pad 2: LVDS0_D2_N -> GND
- C39 pad 2: LVDS0_D2_N -> GND
- C4 pad 2: LVDS0_D2_N -> GND
- C40 pad 2: LVDS0_D2_N -> GND
- C41 pad 2: LVDS0_D2_N -> GND
- C42 pad 2: LVDS0_D2_N -> GND
- C43 pad 2: LVDS0_D2_N -> GND
- C44 pad 2: LVDS0_D2_N -> GND
- C45 pad 2: LVDS0_D2_N -> GND
- C46 pad 2: LVDS0_D2_N -> GND
- C47 pad 2: LVDS0_D2_N -> GND
- C48 pad 2: LVDS0_D2_N -> GND
- C49 pad 2: LVDS0_D2_N -> GND
- C5 pad 2: LVDS0_D2_N -> GND
- C50 pad 2: LVDS0_D2_N -> GND
- C51 pad 2: LVDS0_D2_N -> GND
- C52 pad 2: LVDS0_D2_N -> GND
- C53 pad 2: LVDS0_D2_N -> GND
- C54 pad 2: LVDS0_D2_N -> GND
- C55 pad 2: LVDS0_D2_N -> GND
- C56 pad 2: LVDS0_D2_N -> GND
- C57 pad 2: LVDS0_D2_N -> GND
- C58 pad 2: LVDS0_D2_N -> GND
- C59 pad 2: LVDS0_D2_N -> GND
- C6 pad 2: LVDS0_D2_N -> GND
- C60 pad 2: LVDS0_D2_N -> GND
- C61 pad 2: LVDS0_D2_N -> GND
- C62 pad 2: LVDS0_D2_N -> GND
- C63 pad 2: LVDS0_D2_N -> GND
- C64 pad 2: LVDS0_D2_N -> GND
- C65 pad 2: LVDS0_D2_N -> GND
- C66 pad 2: LVDS0_D2_N -> GND
- C67 pad 2: LVDS0_D2_N -> GND
- C69 pad 2: LVDS0_D2_N -> GND
- C7 pad 1: VDD_SYS -> /power_unit/power_5v/5v
- C7 pad 2: LVDS0_D2_N -> GND
- C70 pad 2: LVDS0_D2_N -> GND
- C72 pad 2: LVDS0_D2_N -> GND
- C73 pad 2: LVDS0_D2_N -> GND
- C74 pad 2: LVDS0_D2_N -> GND
- C75 pad 2: LVDS0_D2_N -> GND
- C76 pad 1: Net-(U17-VCCB) -> /power_unit/power_5v/3v3
- C76 pad 2: LVDS0_D2_N -> GND
- C77 pad 2: LVDS0_D2_N -> GND
- C78 pad 2: LVDS0_D2_N -> GND
- C79 pad 2: LVDS0_D2_N -> GND
- C8 pad 1: VDD_SYS -> /power_unit/power_5v/5v
- C8 pad 2: LVDS0_D2_N -> GND
- C80 pad 2: LVDS0_D2_N -> GND
- C81 pad 2: LVDS0_D2_N -> GND
- C82 pad 2: LVDS0_D2_N -> GND
- C83 pad 2: LVDS0_D2_N -> GND
- C84 pad 2: LVDS0_D2_N -> GND
- C85 pad 2: LVDS0_D2_N -> GND
- C86 pad 2: LVDS0_D2_N -> GND
- C87 pad 2: LVDS0_D2_N -> GND
- C88 pad 2: LVDS0_D2_N -> GND
- C89 pad 2: LVDS0_D2_N -> GND
- C9 pad 1: VDD_SYS -> /power_unit/power_5v/5v
- C9 pad 2: LVDS0_D2_N -> GND
- C90 pad 2: LVDS0_D2_N -> GND
- C91 pad 2: LVDS0_D2_N -> GND
- C92 pad 2: LVDS0_D2_N -> GND
- C93 pad 2: LVDS0_D2_N -> GND
- C94 pad 2: LVDS0_D2_N -> GND
- C95 pad 2: LVDS0_D2_N -> GND
- C96 pad 2: LVDS0_D2_N -> GND
- C97 pad 2: LVDS0_D2_N -> GND
- C98 pad 2: LVDS0_D2_N -> GND
- C99 pad 2: LVDS0_D2_N -> GND
- D1 pad 2: LVDS0_D2_N -> GND
- D10 pad 2: LVDS0_D2_N -> GND
- D11 pad 2: LVDS0_D2_N -> GND
- D12 pad 2: LVDS0_D2_N -> GND
- D5 pad 2: LVDS0_D2_N -> GND
- D6 pad 2: LVDS0_D2_N -> GND
- D7 pad 2: LVDS0_D2_N -> GND
- D8 pad 2: LVDS0_D2_N -> GND
- D9 pad 2: LVDS0_D2_N -> GND
- J10 pad 2: LVDS0_D2_N -> GND
- J11 pad 5: LVDS0_D2_N -> GND
- J18 pad 1: LVDS0_D2_N -> GND
- J19 pad 1: LVDS0_D2_N -> GND
- J20 pad 1: LVDS0_D2_N -> GND
- J21 pad 1: LVDS0_D2_N -> GND
- J3 pad 11: PCIE_TXN_P -> unconnected-(J3-Pad11)
- J3 pad 13: PCIE_TXN_N -> unconnected-(J3-Pad13)
- J3 pad 15: PCIE_RXN_P -> unconnected-(J3-Pad15)
- J3 pad 17: PCIE_RXN_N -> unconnected-(J3-Pad17)
- J3 pad 21: PCIE_REF_PAD_CLK_P -> unconnected-(J3-Pad21)
- J3 pad 23: PCIE_REF_PAD_CLK_N -> unconnected-(J3-Pad23)
- J3 pad 33: GPIO1_IO00 -> unconnected-(J3-Pad33)
- J3 pad 35: GPIO1_IO01 -> unconnected-(J3-Pad35)
- J3 pad 37: GPIO1_IO02 -> unconnected-(J3-Pad37)
- J3 pad 43: GPIO1_IO05 -> unconnected-(J3-Pad43)
- J3 pad 45: GPIO1_IO06 -> unconnected-(J3-Pad45)
- J3 pad 47: GPIO1_IO07 -> unconnected-(J3-Pad47)
- J3 pad 49: GPIO1_IO08 -> unconnected-(J3-Pad49)
- J3 pad 51: GPIO1_IO09 -> unconnected-(J3-Pad51)
- J3 pad 53: GPIO1_IO10 -> unconnected-(J3-Pad53)
- J3 pad 55: GPIO1_IO11 -> unconnected-(J3-Pad55)
- J3 pad 57: GPIO1_IO12 -> unconnected-(J3-Pad57)
- J3 pad 59: GPIO1_IO13 -> unconnected-(J3-Pad59)
- J3 pad 61: GPIO1_IO14 -> unconnected-(J3-Pad61)
- J3 pad 63: GPIO1_IO15 -> unconnected-(J3-Pad63)
- J3 pad 75: LVDS0_D2_N -> GND
- J3 pad 76: LVDS0_D2_N -> GND
- J3 pad 77: LVDS0_D2_N -> GND
- J3 pad 78: LVDS0_D2_N -> GND
- J3 pad 79: LVDS0_D2_N -> GND
- J3 pad 80: LVDS0_D2_N -> GND
- J3 pad 81: LVDS0_D2_N -> GND
- J3 pad 82: LVDS0_D2_N -> GND
- J3 pad 83: LVDS0_D2_N -> GND
- J3 pad 84: LVDS0_D2_N -> GND
- J3 pad 85: LVDS0_D2_N -> GND
- J3 pad 86: LVDS0_D2_N -> GND
- J3 pad 87: LVDS0_D2_N -> GND
- J3 pad 88: LVDS0_D2_N -> GND
- J4 pad 47: LVDS0_D2_N -> LVDS1_D2_N
- J4 pad 59: LVDS0_CLK_P -> unconnected-(J4-Pad59)
- J4 pad 61: LVDS0_CLK_N -> unconnected-(J4-Pad61)
- J4 pad 63: LVDS0_D3_P -> unconnected-(J4-Pad63)
- J4 pad 65: LVDS0_D3_N -> unconnected-(J4-Pad65)
- J4 pad 67: LVDS0_D2_P -> unconnected-(J4-Pad67)
- J4 pad 69: LVDS0_D2_N -> unconnected-(J4-Pad69)
- J4 pad 71: LVDS0_D1_P -> unconnected-(J4-Pad71)
- J4 pad 73: LVDS0_D1_N -> unconnected-(J4-Pad73)
- J4 pad 75: LVDS0_D0_P -> unconnected-(J4-Pad75)
- J4 pad 77: LVDS0_D0_N -> unconnected-(J4-Pad77)
- J9 pad 13: LVDS0_D2_N -> GND
- J9 pad 16: LVDS0_D2_N -> GND
- J9 pad 4: LVDS0_D2_N -> GND
- J9 pad 7: LVDS0_D2_N -> GND
- L1 pad 1: VDD_SYS -> /power_unit/power_5v/5v
- R1 pad 1: /power_unit/power_5v/5V_EN -> Net-(U20-IN-)
- R1 pad 2: Net-(Q1B-GP) -> VDD_SYS
- R13 pad 2: LVDS0_D2_N -> GND
- R15 pad 1: Net-(U4-SENSE) -> +V_SUPPLY_FILT
- R15 pad 2: /power_unit/+V_SUPPLY_FILT -> Net-(U4-SENSE)
- R16 pad 1: /power_unit/power_3V3_1V8_1V2/5V_EN -> unconnected-(R16-Pad1)
- R16 pad 2: Net-(Q4B-GP) -> unconnected-(R16-Pad2)
- R17 pad 1: /power_unit/power_3V3_1V8_1V2/+V5_STB -> Net-(J25-Pin_2)
- R17 pad 2: Net-(Q4B-GP) -> /OutGPIO_CAN/GND_CAN2
- R18 pad 1: Net-(Q4B-DP) -> +V5_STB
- R18 pad 2: LVDS0_D2_N -> GND
- R2 pad 1: /power_unit/power_5v/+V5_STB -> Net-(U20-IN+)
- R2 pad 2: Net-(Q1B-GP) -> /power_unit/power_5v/5v
- R20 pad 2: LVDS0_D2_N -> GND
- R21 pad 2: LVDS0_D2_N -> GND
- R22 pad 1: /power_unit/power_3V3_1V8_1V2/+V_SUPPLY_FILT -> +V_SUPPLY_FILT
- R27 pad 1: unconnected-(R27-Pad1) -> Net-(J24-Pin_2)
- R27 pad 2: unconnected-(R27-Pad2) -> /OutGPIO_CAN/GND_CAN1
- R29 pad 2: LVDS0_D2_N -> GND
- R3 pad 1: Net-(Q1B-DP) -> +V5_STB
- R3 pad 2: LVDS0_D2_N -> GND
- R31 pad 2: LVDS0_D2_N -> GND
- R34 pad 2: LVDS0_D2_N -> GND
- R35 pad 2: LVDS0_D2_N -> GND
- R36 pad 2: LVDS0_D2_N -> GND
- R37 pad 2: LVDS0_D2_N -> GND
- R38 pad 2: LVDS0_D2_N -> GND
- R4 pad 1: VDD_SYS -> /power_unit/power_5v/5v
- R43 pad 2: LVDS0_D2_N -> GND
- R46 pad 2: LVDS0_D2_N -> GND
- R48 pad 2: LVDS0_D2_N -> GND
- R49 pad 2: LVDS0_D2_N -> GND
- R5 pad 2: LVDS0_D2_N -> GND
- R52 pad 2: LVDS0_D2_N -> GND
- R53 pad 2: LVDS0_D2_N -> GND
- R54 pad 2: LVDS0_D2_N -> GND
- R55 pad 2: LVDS0_D2_N -> GND
- R58 pad 1: LVDS0_D2_N -> GND
- R6 pad 2: LVDS0_D2_N -> GND
- R61 pad 2: Net-(U13-ILIM) -> unconnected-(R61-Pad2)
- R7 pad 2: /power_unit/+V5_STB -> +V5_STB
- R8 pad 1: /power_unit/power_5v/+V_SUPPLY_FILT -> +V_SUPPLY_FILT
- SW1 pad 1: LVDS0_D2_N -> GND
- SW1 pad 2: LVDS0_D2_N -> GND
- SW2 pad 1: LVDS0_D2_N -> GND
- SW2 pad 2: LVDS0_D2_N -> GND
- SW3 pad 1: LVDS0_D2_N -> GND
- SW3 pad 2: LVDS0_D2_N -> GND
- U1 pad 29: LVDS0_D2_N -> GND
- U1 pad 49: LVDS0_D2_N -> GND
- U10 pad B1: LVDS0_D2_N -> GND
- U10 pad B2: LVDS0_D2_N -> GND
- U10 pad B3: LVDS0_D2_N -> GND
- U11 pad 13: LVDS0_D2_N -> GND
- U11 pad 7: LVDS0_D2_N -> GND
- U12 pad 13: LVDS0_D2_N -> GND
- U12 pad 7: LVDS0_D2_N -> GND
- U13 pad 13: LVDS0_D2_N -> GND
- U13 pad 7: LVDS0_D2_N -> GND
- U13 pad 8: Net-(U13-ILIM) -> unconnected-(U13-ILIM-Pad8)
- U14 pad 4: LVDS0_D2_N -> GND
- U15 pad 4: LVDS0_D2_N -> GND
- U16 pad 4: LVDS0_D2_N -> GND
- U17 pad 4: LVDS0_D2_N -> GND
- U17 pad 8: Net-(U17-VCCB) -> /power_unit/power_5v/3v3
- U18 pad 4: LVDS0_D2_N -> GND
- U19 pad 4: LVDS0_D2_N -> GND
- U20 pad 5: Net-(U20-VS) -> /power_unit/power_5v/3v3
- U20 pad 6: LVDS0_D2_N -> GND
- U21 pad B1: LVDS0_D2_N -> GND
- U21 pad B2: LVDS0_D2_N -> GND
- U21 pad B3: LVDS0_D2_N -> GND
- U22 pad A3: (no net) -> Net-(U22B-CH2_IN+)
- U22 pad A4: (no net) -> Net-(U22B-CH2_IN-)
- U22 pad B1: LVDS0_D2_N -> GND
- U22 pad B2: (no net) -> GND
- U22 pad C3: (no net) -> Net-(U22B-CH2_OUT+)
- U22 pad C4: (no net) -> Net-(U22B-CH2_OUT-)
- U23 pad B1: LVDS0_D2_N -> GND
- U24 pad 3: LVDS0_D2_N -> GND
- U24 pad 4: /Ethernet/ETH2_MDI1+ -> /Ethernet/ETH2_MDI1-
- U24 pad 5: /Ethernet/ETH2_MDI1- -> /Ethernet/ETH2_MDI1+
- U24 pad 8: LVDS0_D2_N -> GND
- U25 pad 3: LVDS0_D2_N -> GND
- U25 pad 4: /Ethernet/ETH2_MDI3+ -> /Ethernet/ETH2_MDI3-
- U25 pad 5: /Ethernet/ETH2_MDI3- -> /Ethernet/ETH2_MDI3+
- U25 pad 8: LVDS0_D2_N -> GND
- U26 pad 3: LVDS0_D2_N -> GND
- U26 pad 4: ETH1_MDI1+ -> ETH1_MDI1-
- U26 pad 5: ETH1_MDI1- -> ETH1_MDI1+
- U26 pad 8: LVDS0_D2_N -> GND
- U27 pad 3: LVDS0_D2_N -> GND
- U27 pad 4: ETH1_MDI3+ -> ETH1_MDI3-
- U27 pad 5: ETH1_MDI3- -> ETH1_MDI3+
- U27 pad 8: LVDS0_D2_N -> GND
- U28 pad 3: LVDS0_D2_N -> GND
- U28 pad 8: LVDS0_D2_N -> GND
- U29 pad 3: LVDS0_D2_N -> GND
- U29 pad 8: LVDS0_D2_N -> GND
- U3 pad 57: LVDS0_D2_N -> GND
- U30 pad 12: LVDS0_D2_N -> GND
- U30 pad 18: LVDS0_D2_N -> GND
- U30 pad 24: LVDS0_D2_N -> GND
- U30 pad 28: LVDS0_D2_N -> GND
- U30 pad 33: LVDS0_D2_N -> GND
- U31 pad 1: LVDS0_D2_N -> GND
- U31 pad 10: LVDS0_D2_N -> GND
- U31 pad 11: LVDS0_D2_N -> GND
- U31 pad 12: unconnected-(U31-VCORE-Pad12) -> /serial_interface/1v8_VREGOUT
- U31 pad 13: unconnected-(U31-TEST-Pad13) -> GND
- U31 pad 14: unconnected-(U31-~{RESET}-Pad14) -> Net-(U31-~{RESET})
- U31 pad 15: LVDS0_D2_N -> GND
- U31 pad 2: unconnected-(U31-OSCI-Pad2) -> Net-(U31-OSCI)
- U31 pad 20: unconnected-(U31-VCCIO-Pad20) -> Net-(C163-Pad1)
- U31 pad 25: LVDS0_D2_N -> GND
- U31 pad 3: unconnected-(U31-OSCO-Pad3) -> Net-(U31-OSCO)
- U31 pad 31: unconnected-(U31-VCCIO-Pad31) -> Net-(C163-Pad1)
- U31 pad 35: LVDS0_D2_N -> GND
- U31 pad 37: unconnected-(U31-VCORE-Pad37) -> /serial_interface/1v8_VREGOUT
- U31 pad 4: unconnected-(U31-VPHY-Pad4) -> /serial_interface/VPHY
- U31 pad 42: unconnected-(U31-VCCIO-Pad42) -> Net-(C163-Pad1)
- U31 pad 47: LVDS0_D2_N -> GND
- U31 pad 49: unconnected-(U31-VREGOUT-Pad49) -> /serial_interface/1v8_VREGOUT
- U31 pad 5: LVDS0_D2_N -> GND
- U31 pad 50: unconnected-(U31-VREGIN-Pad50) -> /serial_interface/3v3
- U31 pad 51: LVDS0_D2_N -> GND
- U31 pad 56: unconnected-(U31-VCCIO-Pad56) -> Net-(C163-Pad1)
- U31 pad 6: unconnected-(U31-REF-Pad6) -> Net-(U31-REF)
- U31 pad 61: unconnected-(U31-EEDATA-Pad61) -> /serial_interface/EEDATA
- U31 pad 62: unconnected-(U31-EECLK-Pad62) -> /serial_interface/EECLK
- U31 pad 63: unconnected-(U31-EECS-Pad63) -> /serial_interface/EECS
- U31 pad 64: unconnected-(U31-VCORE-Pad64) -> /serial_interface/1v8_VREGOUT
- U31 pad 7: unconnected-(U31-DM-Pad7) -> Net-(U22B-CH2_OUT+)
- U31 pad 8: unconnected-(U31-DP-Pad8) -> Net-(U22B-CH2_OUT-)
- U31 pad 9: unconnected-(U31-VPLL-Pad9) -> /serial_interface/VPLL
- U33 pad 1: unconnected-(U33-VDD1-Pad1) -> /OutGPIO_CAN/1v8_CAN
- U33 pad 2: Net-(U33-GND1-Pad2) -> unconnected-(U33-TXD-Pad2)
- U33 pad 4: unconnected-(U33-NC-Pad4) -> GND
- U33 pad 5: unconnected-(U33-RXD-Pad5) -> Net-(J25-Pin_4)
- U33 pad 6: unconnected-(U33-NC-Pad6) -> Net-(J25-Pin_3)
- U33 pad 7: Net-(U33-GND1-Pad2) -> /OutGPIO_CAN/GND_CAN2
- U33 pad 8: Net-(U33-GND1-Pad2) -> /OutGPIO_CAN/5v_CAN2
- U4 pad 11: LVDS0_D2_N -> GND
- U4 pad 5: LVDS0_D2_N -> GND
- U4 pad 8: Net-(U4-SENSE) -> +V_SUPPLY_FILT
- U5 pad 12: LVDS0_D2_N -> GND
- U5 pad 13: LVDS0_D2_N -> GND
- U5 pad 14: LVDS0_D2_N -> GND
- U5 pad 15: LVDS0_D2_N -> GND
- U5 pad 19: LVDS0_D2_N -> GND
- U5 pad 2: Net-(Q1B-DP) -> +V5_STB
- U5 pad 4: LVDS0_D2_N -> GND
- U5 pad 7: /power_unit/power_5v/+V_SUPPLY_FILT -> +V_SUPPLY_FILT
- U5 pad 8: /power_unit/power_5v/+V_SUPPLY_FILT -> +V_SUPPLY_FILT
- U5 pad 9: /power_unit/power_5v/+V_SUPPLY_FILT -> +V_SUPPLY_FILT
- U6 pad 1: /power_unit/+V_SUPPLY_FILT -> +V_SUPPLY_FILT
- U6 pad 2: LVDS0_D2_N -> GND
- U6 pad 3: /power_unit/+V5_STB -> +V5_STB
- U6 pad 4: LVDS0_D2_N -> GND
- U7 pad 12: LVDS0_D2_N -> GND
- U7 pad 13: LVDS0_D2_N -> GND
- U7 pad 14: LVDS0_D2_N -> GND
- U7 pad 15: LVDS0_D2_N -> GND
- U7 pad 19: LVDS0_D2_N -> GND
- U7 pad 2: Net-(Q4B-DP) -> +V5_STB
- U7 pad 4: LVDS0_D2_N -> GND
- U7 pad 7: /power_unit/power_3V3_1V8_1V2/+V_SUPPLY_FILT -> +V_SUPPLY_FILT
- U7 pad 8: /power_unit/power_3V3_1V8_1V2/+V_SUPPLY_FILT -> +V_SUPPLY_FILT
- U7 pad 9: /power_unit/power_3V3_1V8_1V2/+V_SUPPLY_FILT -> +V_SUPPLY_FILT
- U8 pad 1: LVDS0_D2_N -> GND
- U8 pad 3: /power_unit/+V5_STB -> +V5_STB
- U8 pad 4: /power_unit/+V5_STB -> +V5_STB
- U8 pad 9: LVDS0_D2_N -> GND
- U9 pad B1: LVDS0_D2_N -> GND
- U9 pad B2: LVDS0_D2_N -> GND
- U9 pad B3: LVDS0_D2_N -> GND
- Y1 pad 2: LVDS0_D2_N -> GND
- Y1 pad 4: LVDS0_D2_N -> GND
- Y2 pad 2: LVDS0_D2_N -> GND
- Y2 pad 4: LVDS0_D2_N -> GND
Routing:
- net GND: track 0.00 -> 47.7 mm, vias 0 -> 1
- net /power_unit/+V_SUPPLY_FILT: track 30.4 -> 0.00 mm, vias 2 -> 0
- net Net-(U4-GATE): track 30.2 -> 1.30 mm, vias 2 -> 0
- net (no net): track 24.1 -> 0.00 mm
- net /Ethernet/ETH2_MDI1-: track 0.00 -> 20.1 mm
- net +V_SUPPLY_FILT: track 0.00 -> 19.9 mm
- net /Ethernet/ETH2_MDI1+: track 0.00 -> 17.8 mm
- net /Ethernet/ETH2_MDI2-: track 0.00 -> 17.2 mm
- net /Ethernet/ETH2_MDI2+: track 0.00 -> 16.6 mm
- net /Ethernet/ETH2_MDI3-: track 0.00 -> 16.5 mm
- net Net-(Q1B-GP): track 16.4 -> 0.00 mm, vias 1 -> 0
- net /Ethernet/ETH2_MDI0-: track 0.00 -> 16.4 mm
- net /Ethernet/ETH2_MDI0+: track 0.00 -> 15.8 mm
- net VDD_SYS: track 23.0 -> 7.24 mm, vias 1 -> 0
- net +V5_STB: track 0.00 -> 15.4 mm
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- added copper zone on F.Cu, net /power_unit/V_IN
- added copper zone on In1.Cu, net GND
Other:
- board size 125 x 100 mm -> 149.8 x 124.9 mm
- copper layers 2 -> 4
